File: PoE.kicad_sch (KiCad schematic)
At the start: 80 parts, among them Q2 BSZ440N10NS3GATMA1, T1 PA2467NL, U23 TPS23734, U24 TCMT1107

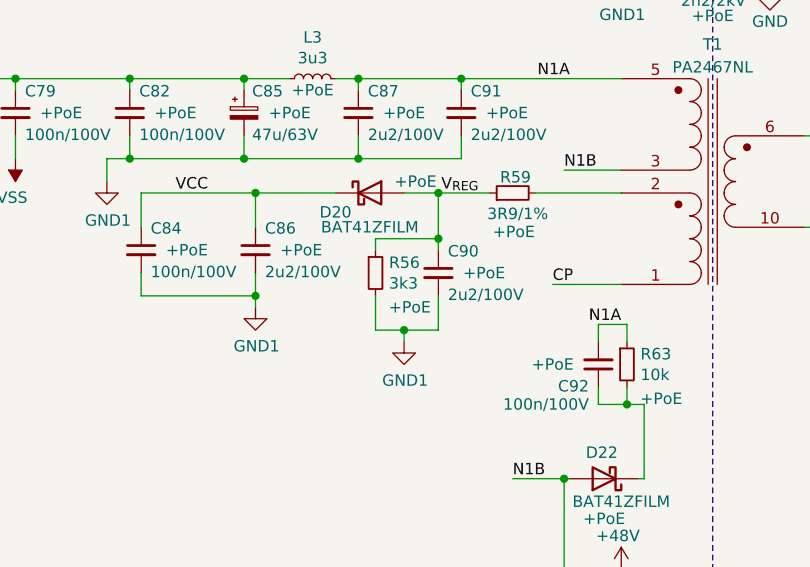
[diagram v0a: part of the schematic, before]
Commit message: Change rating of PoE capacitors to 2.2uF/25V
2.2uF/100V are not really available in a 0805 package. This part of
the PoE design a 25V rating is sufficent.

Fixes: #22

Signed-off-by: Stefan Agner <stefan@agner.ch>
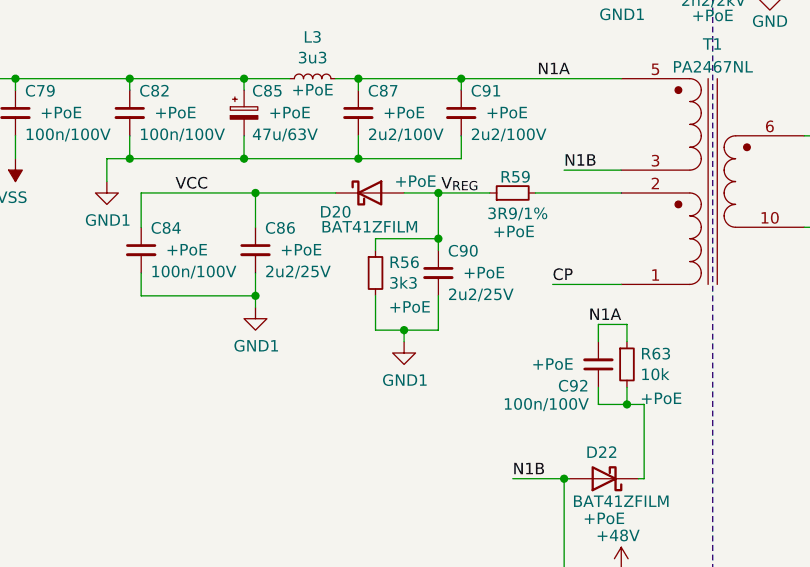
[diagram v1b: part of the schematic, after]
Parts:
- C86, C90: value 2u2/100V -> 2u2/25V
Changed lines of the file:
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@@
       (effects (font (size 1.27 1.27)) (justify left))
     )
-    (property "Value" "2u2/100V" (id 1) (at 149.644 57.029 0)
+    (property "Value" "2u2/25V" (id 1) (at 149.644 57.029 0)
       (effects (font (size 1.27 1.27)) (justify left))
     )
@@
       (effects (font (size 1.27 1.27)) (justify left))
     )
-    (property "Value" "2u2/100V" (id 1) (at 169.964 59.569 0)
+    (property "Value" "2u2/25V" (id 1) (at 169.964 59.569 0)
       (effects (font (size 1.27 1.27)) (justify left))
     )

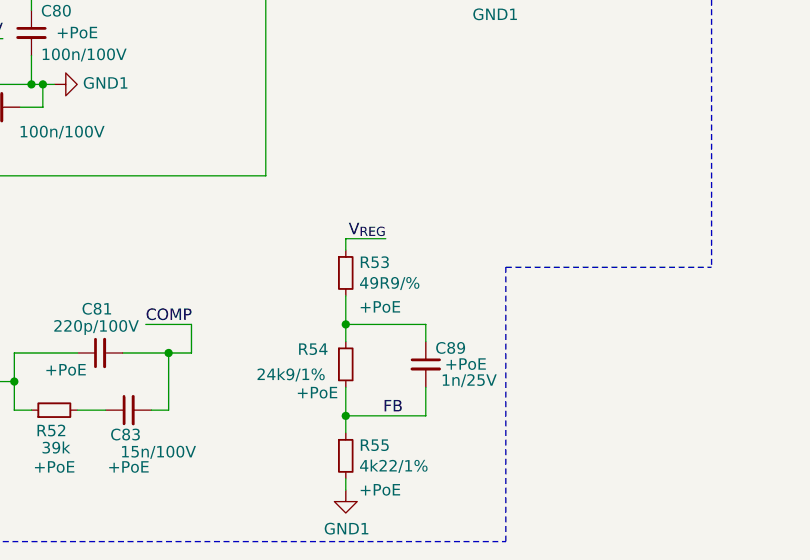
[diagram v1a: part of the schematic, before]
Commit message: Clarify rating of C52/R53
C52 needs to be 100n/25V, R53 should be 1% accuracy.

Signed-off-by: Stefan Agner <stefan@agner.ch>
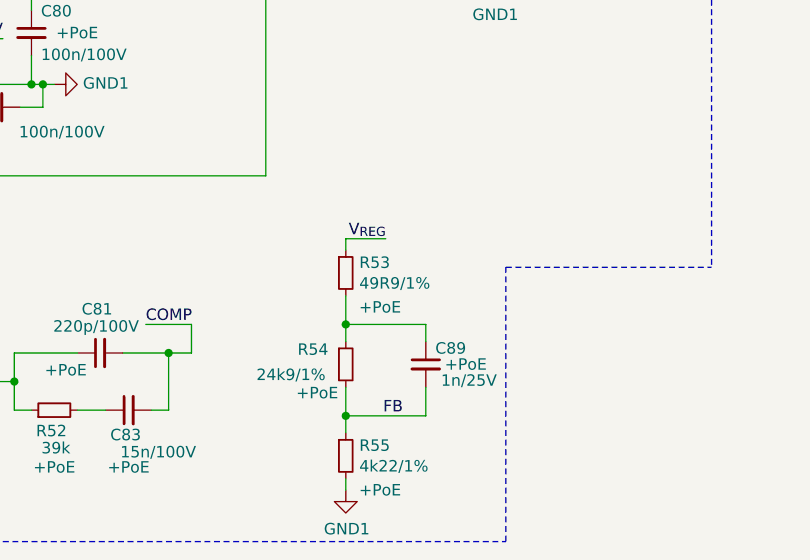
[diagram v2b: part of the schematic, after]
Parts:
- R53: value 49R9/% -> 49R9/1%
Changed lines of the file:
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@@
       (effects (font (size 1.27 1.27)) (justify left))
     )
-    (property "Value" "49R9/%" (id 1) (at 160.249 166.884 0)
+    (property "Value" "49R9/1%" (id 1) (at 160.249 166.884 0)
       (effects (font (size 1.27 1.27)) (justify left))
     )

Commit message: Change footprint of C87/C91 to 1206
2.2uF/100V don't really exist in 0805 package. Use 1206 package for
those capacitors.

Fixes: #21

Signed-off-by: Stefan Agner <stefan@agner.ch>
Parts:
- C87, C91: footprint Capacitor_SMD:C_0805_2012Metric -> Capacitor_SMD:C_1206_3216Metric
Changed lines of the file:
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@@
       (effects (font (size 1.27 1.27)) (justify left))
     )
-    (property "Footprint" "Capacitor_SMD:C_0805_2012Metric" (id 2) (at 160.02 39.37 0)
+    (property "Footprint" "Capacitor_SMD:C_1206_3216Metric" (id 2) (at 160.02 39.37 0)
       (effects (font (size 1.27 1.27)) hide)
     )
@@
       (effects (font (size 1.27 1.27)) (justify left))
     )
-    (property "Footprint" "Capacitor_SMD:C_0805_2012Metric" (id 2) (at 171.45 39.37 0)
+    (property "Footprint" "Capacitor_SMD:C_1206_3216Metric" (id 2) (at 171.45 39.37 0)
       (effects (font (size 1.27 1.27)) hide)
     )

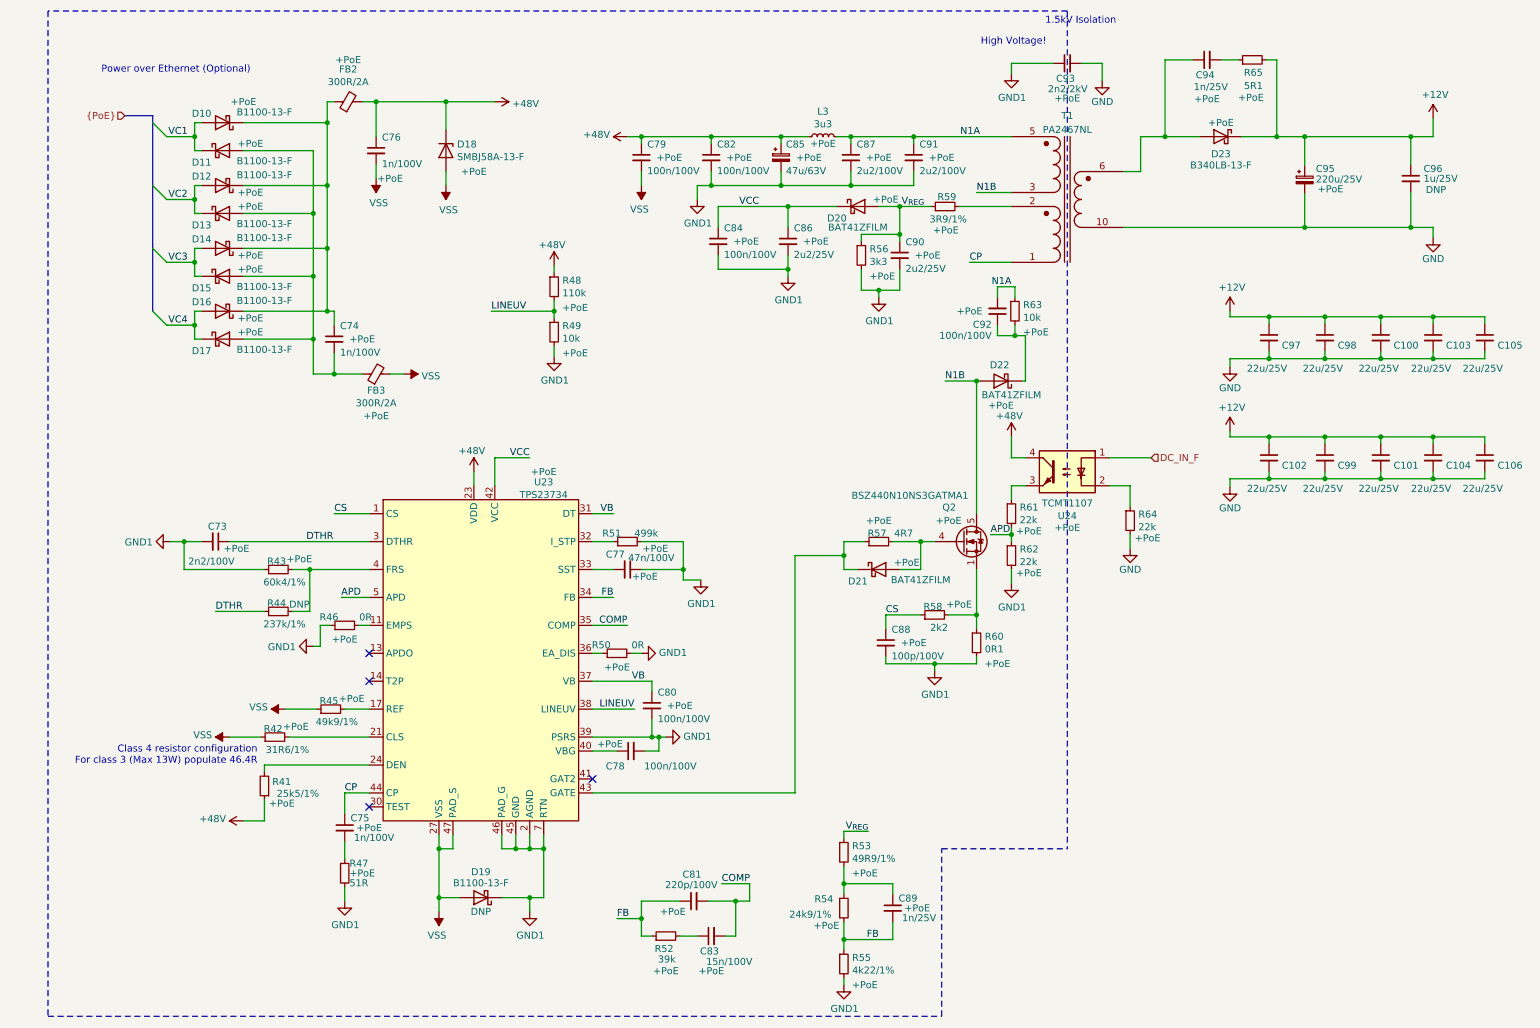
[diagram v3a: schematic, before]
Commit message: initial rev 0.3:
updates
schematic:
-change usb current protection IC to 1.5A
-Added low-pass filter to the audio output
-PoE fixed primary windings polarity
-added option to select poe class with a jumper (between 3 and 4)
-fixes in poe design
-added testpoints
-added virtual hirose df40c connectors for pick and place use

lightblue.pretty:
-added fake DF40C footprint for pick and place and 3d model purposes

Signed-off-by: Dominik Sliwa <dominik@sliwa.io>
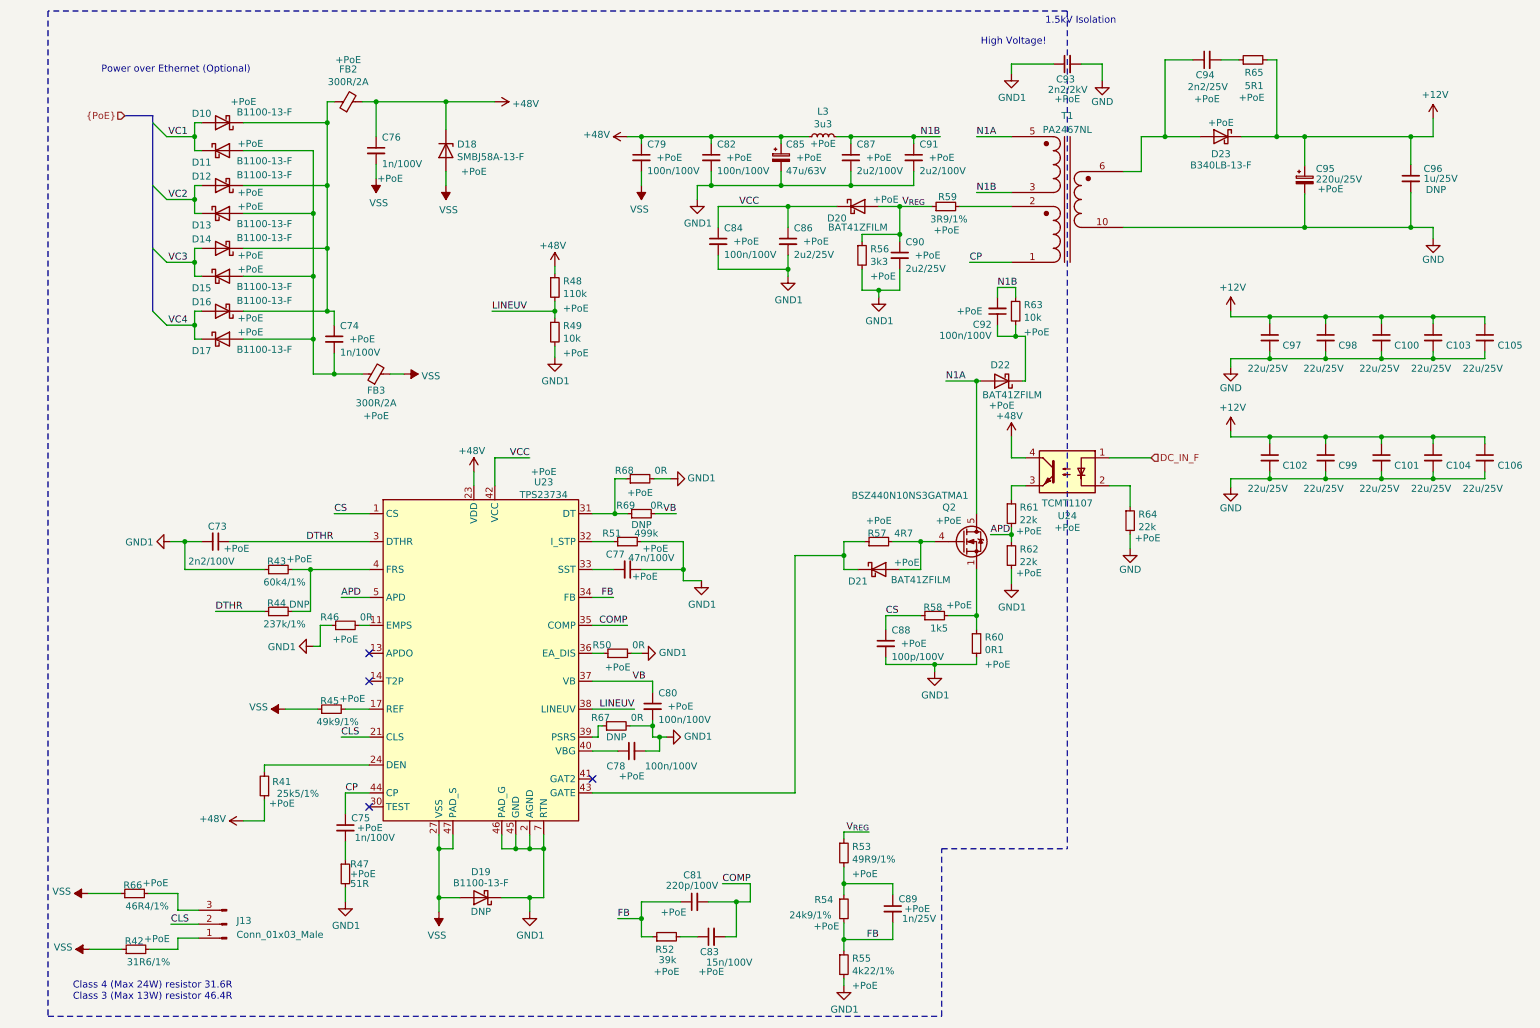
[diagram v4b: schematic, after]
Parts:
- added J13: Conn_01x03_Male, Connector_PinHeader_2.54mm:PinHeader_1x03_P2.54mm_Vertical, symbol Connector:Conn_01x03_Male
- added R66: 46R4/1%, Resistor_SMD:R_0402_1005Metric, symbol Device:R_Small
- added R67, R68, R69: 0R, Resistor_SMD:R_0402_1005Metric, symbol Device:R_Small
- C94: value 1n/25V -> 2n2/25V
- R57: footprint Resistor_SMD:R_0402_1005Metric -> Resistor_SMD:R_0805_2012Metric
- R58: value 2k2 -> 1k5
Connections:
- net GND1: now also R67.2, R68.2; no longer U23.39 (PSRS)
- net N1A: now also D22.2 (A), Q2.5 (D); no longer C87.1, C91.1, C92.2, L3.2, R63.1
- net N1B: now also C87.1, C91.1, C92.2, L3.2, R63.1; no longer D22.2 (A), Q2.5 (D)
- net VB: now also R69.2; no longer U23.31 (DT)
- net VSS: now also R66.1
- net at R42.2: now also J13.1 (Pin_1); no longer U23.21 (CLS)
- new net: R68.1, R69.1, U23.31 (DT)
- new net: R67.1, U23.39 (PSRS)
- new net: J13.3 (Pin_3), R66.2
- new net CLS: J13.2 (Pin_2), U23.21 (CLS)
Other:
- note added: "Class 4 (Max 24W) resistor 31.6R Class 3 (Max 13W) resistor 46.4R"
- note removed: "Class 4 resistor configuration For class 3 (Max 13W) populate 46.4R"
- moved on the sheet: R42

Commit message: Renmae LightBlue to Amber
Signed-off-by: Stefan Agner <stefan@agner.ch>
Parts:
- Q2: footprint LightBlue:PG-TSDSON-8 -> Amber:PG-TSDSON-8
- T1: footprint LightBlue:Transformer_Pulse_PA2467NL -> Amber:Transformer_Pulse_PA2467NL; symbol LightBlue:Transformer_Pulse_PA2476NL -> Amber:Transformer_Pulse_PA2476NL
- U23: footprint LightBlue:Texas_VQFN-47-2EP_5x7mm_P0.4mm_ThermalVias -> Amber:Texas_VQFN-47-2EP_5x7mm_P0.4mm_ThermalVias; symbol LightBlue:TPS23734 -> Amber:TPS23734
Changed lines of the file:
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@@
     (company "Nabu Casa")
     (comment 1 "www.nabucasa.com")
-    (comment 2 "Light Blue")
+    (comment 2 "Amber")
   )
   (junction (at 38.862 109.22) (diameter 0.9144) (color 0 0 0 0))
@@
       (effects (font (size 1.27 1.27)) (justify left))
     )
-    (property "Footprint" "LightBlue:PG-TSDSON-8" (id 2) (at 185.42 111.125 0)
+    (property "Footprint" "Amber:PG-TSDSON-8" (id 2) (at 185.42 111.125 0)
       (effects (font (size 1.27 1.27) italic) (justify left) hide)
     )
@@
     (pin "4")
   )
-  (symbol (lib_id "LightBlue:Transformer_Pulse_PA2476NL") (at 199.39 45.72 0) (unit 1)
+  (symbol (lib_id "Amber:Transformer_Pulse_PA2476NL") (at 199.39 45.72 0) (unit 1)
     (in_bom yes) (on_board yes) (fields_autoplaced)
     (property "Reference" "T1" (id 0) (at 199.39 31.75 0))
     (property "Value" "PA2467NL" (id 1) (at 199.39 34.29 0))
-    (property "Footprint" "LightBlue:Transformer_Pulse_PA2467NL" (id 2) (at 199.39 45.72 0)
+    (property "Footprint" "Amber:Transformer_Pulse_PA2467NL" (id 2) (at 199.39 45.72 0)
       (effects (font (size 1.27 1.27)) hide)
     )
@@
     (pin "6")
   )
-  (symbol (lib_id "LightBlue:TPS23734") (at 92.71 130.81 0) (unit 1)
+  (symbol (lib_id "Amber:TPS23734") (at 92.71 130.81 0) (unit 1)
     (in_bom yes) (on_board yes)
     (property "Reference" "U23" (id 0) (at 104.14 98.4058 0))
     (property "Value" "TPS23734" (id 1) (at 104.14 100.7045 0))
-    (property "Footprint" "LightBlue:Texas_VQFN-47-2EP_5x7mm_P0.4mm_ThermalVias" (id 2) (at 92.71 134.62 0)
+    (property "Footprint" "Amber:Texas_VQFN-47-2EP_5x7mm_P0.4mm_ThermalVias" (id 2) (at 92.71 134.62 0)
       (effects (font (size 1.27 1.27)) hide)
     )

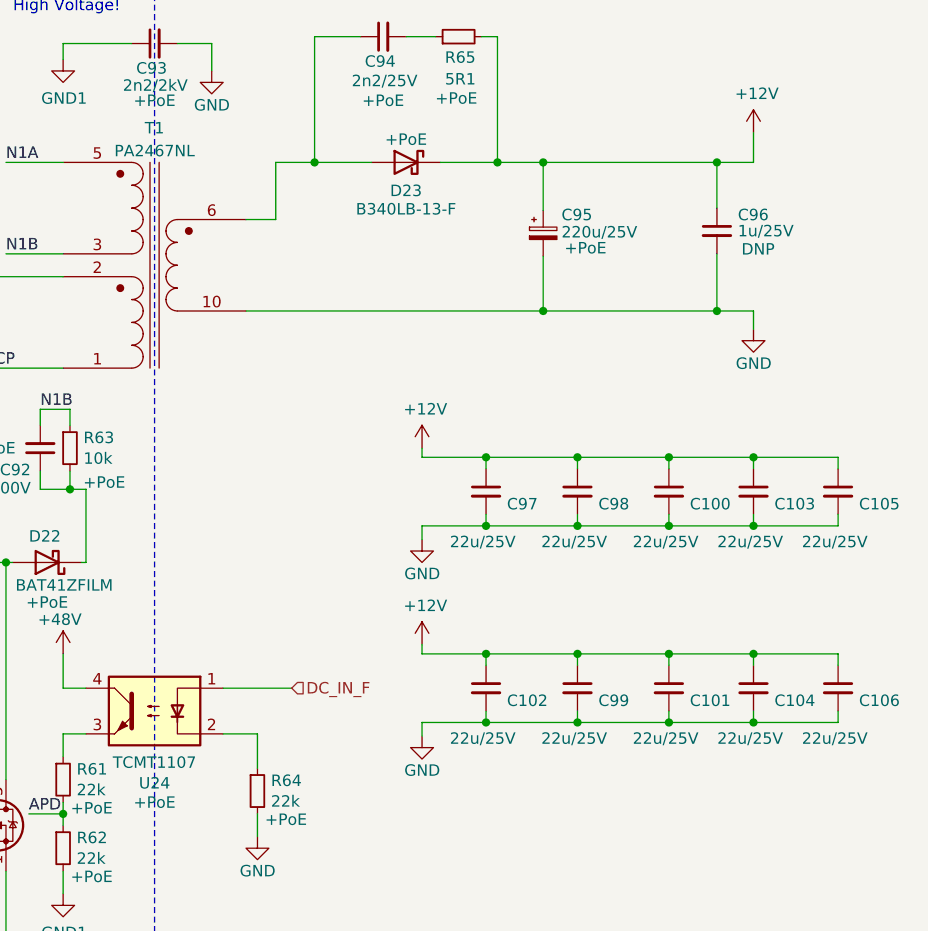
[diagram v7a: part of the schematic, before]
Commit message: Set Config correctly for PoE only parts
Fixes: #34

Signed-off-by: Stefan Agner <stefan@agner.ch>
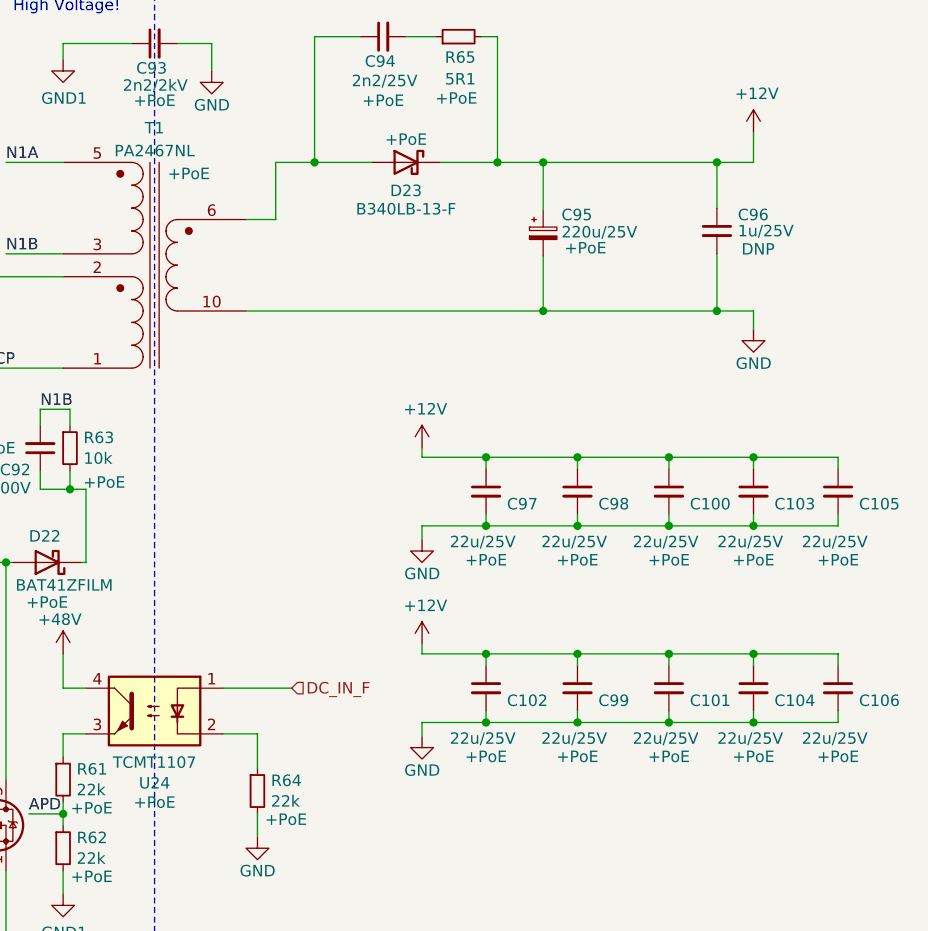
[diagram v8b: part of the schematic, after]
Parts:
- C100, C101, C102, C103, C104, C105, C106, C97, C98, C99, T1: Config (none) -> +PoE
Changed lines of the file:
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@@
       (effects (font (size 1.27 1.27)) hide)
     )
+    (property "Config" "+PoE" (id 4) (at 236.22 79.756 0))
     (pin "1")
     (pin "2")
@@
       (effects (font (size 1.27 1.27)) hide)
     )
+    (property "Config" "+PoE" (id 4) (at 236.22 101.6 0))
     (pin "1")
     (pin "2")
@@
       (effects (font (size 1.27 1.27)) hide)
     )
+    (property "Config" "+PoE" (id 4) (at 246.38 79.756 0))
     (pin "1")
     (pin "2")
@@
       (effects (font (size 1.27 1.27)) hide)
     )
+    (property "Config" "+PoE" (id 4) (at 246.38 101.6 0))
     (pin "1")
     (pin "2")
@@
       (effects (font (size 1.27 1.27)) hide)
     )
+    (property "Config" "+PoE" (id 4) (at 256.54 79.756 0))
     (pin "1")
     (pin "2")
@@
       (effects (font (size 1.27 1.27)) hide)
     )
+    (property "Config" "+PoE" (id 4) (at 256.54 101.6 0))
     (pin "1")
     (pin "2")
@@
       (effects (font (size 1.27 1.27)) hide)
     )
+    (property "Config" "+PoE" (id 4) (at 265.938 79.756 0))
     (pin "1")
     (pin "2")
@@
       (effects (font (size 1.27 1.27)) hide)
     )
+    (property "Config" "+PoE" (id 4) (at 265.938 101.6 0))
     (pin "1")
     (pin "2")
@@
       (effects (font (size 1.27 1.27)) hide)
     )
+    (property "Config" "+PoE" (id 4) (at 275.336 79.756 0))
     (pin "1")
     (pin "2")
@@
       (effects (font (size 1.27 1.27)) hide)
     )
+    (property "Config" "+PoE" (id 4) (at 275.336 101.6 0))
     (pin "1")
     (pin "2")
@@
   )
   (symbol (lib_id "Amber:Transformer_Pulse_PA2476NL") (at 199.39 45.72 0) (unit 1)
-    (in_bom yes) (on_board yes) (fields_autoplaced)
+    (in_bom yes) (on_board yes)
     (property "Reference" "T1" (id 0) (at 199.39 31.75 0))
     (property "Value" "PA2467NL" (id 1) (at 199.39 34.29 0))
@@
       (effects (font (size 1.27 1.27)) hide)
     )
+    (property "Config" "+PoE" (id 6) (at 203.2 36.83 0))
     (pin "1")
     (pin "10")
